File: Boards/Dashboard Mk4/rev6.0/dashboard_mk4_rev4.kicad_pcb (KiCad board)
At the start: 2 copper layers, 82.4 x 41.8 mm, 58 parts, among them J1 MM_F_VT_10, J2 MM_F_VT_20, J3 MM_F_VT_04, J4 CONN_02X03, J5 CONN_02X03, U1 ATMEGA16M1, U2 TPS561201, U3 ATmega328P-AU, U4 CAN_Transceiver, Y1 Crystal_SMD, Y2 Crystal_SMD

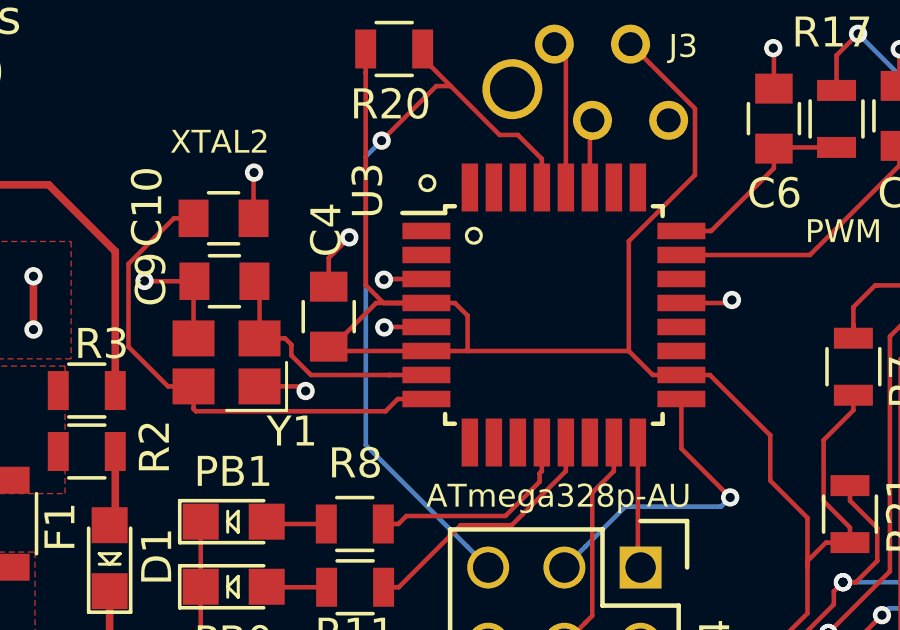
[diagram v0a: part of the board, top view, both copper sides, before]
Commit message: Added interface board
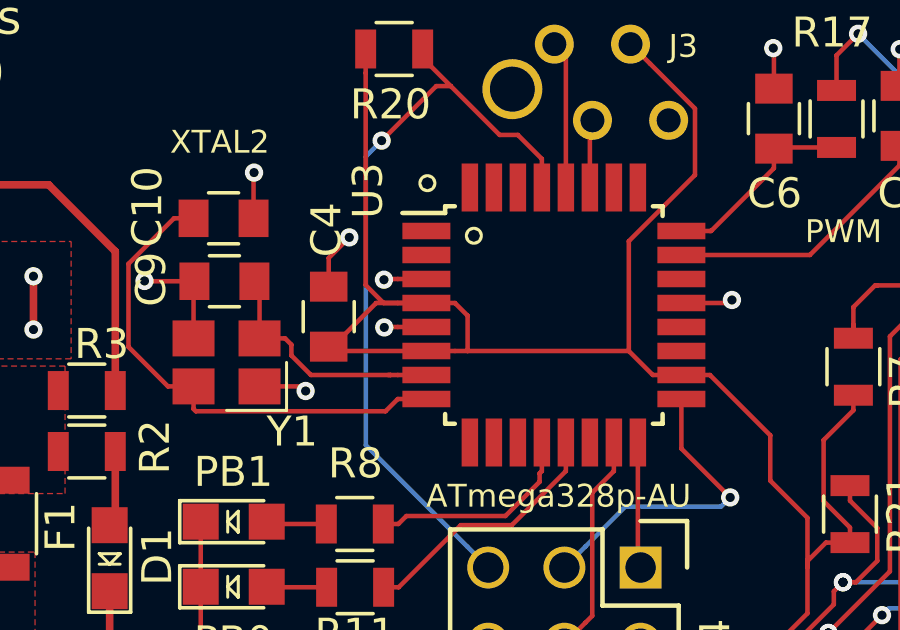
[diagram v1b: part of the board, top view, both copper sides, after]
